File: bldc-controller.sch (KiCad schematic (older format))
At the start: 14 parts, among them U1 STM32F401CBUx

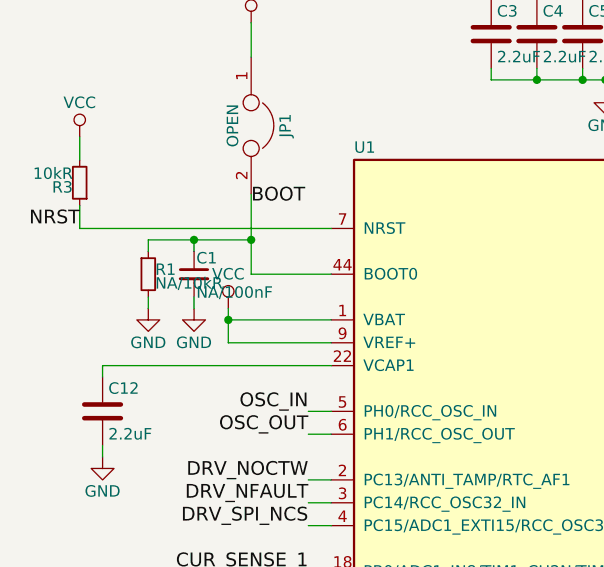
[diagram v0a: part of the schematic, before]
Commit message: even though Im pretty sure that resistor is actually not needed Id like to play safe and have it anyway
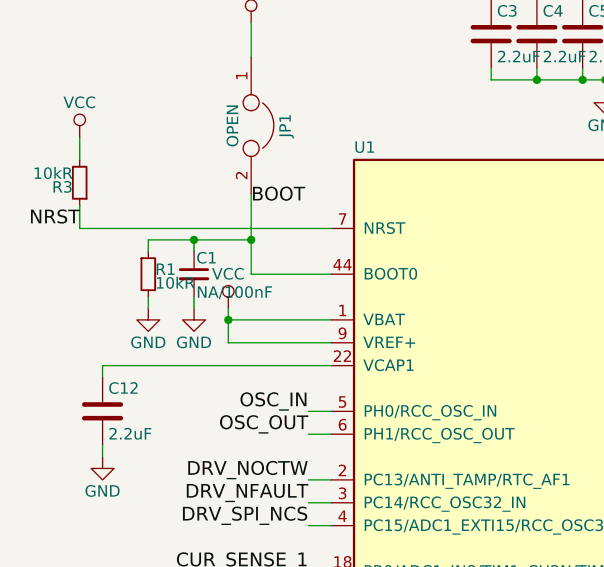
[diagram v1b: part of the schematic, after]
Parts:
- R1: value NA/10kR -> 10kR
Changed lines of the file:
@@
 P 1000 2050
 F 0 "R1" H 1030 2070 50  0000 L CNN
-F 1 "NA/10kR" H 1030 2010 50  0000 L CNN
+F 1 "10kR" H 1030 2010 50  0000 L CNN
 F 2 "Resistors_SMD:R_0603" H 1000 2050 50  0001 C CNN
 F 3 "" H 1000 2050 50  0000 C CNN

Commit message: long forgotten commit of something I did half a year ago -.-
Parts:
- removed JP1: OPEN, Resistors_SMD:R_0402, symbol JUMPER
- added R15: 10kR, Resistor_SMD:R_0603_1608Metric, symbol bldc-controller-rescue:R_Small
- C1: footprint Capacitors_SMD:C_0603 -> Capacitor_SMD:C_0603_1608Metric; symbol C_Small -> bldc-controller-rescue:C_Small
- C10, C12, C3, C4, C5, C6, C7: footprint Capacitors_SMD:C_0603 -> Capacitor_SMD:C_0603_1608Metric; symbol C -> bldc-controller-rescue:C
- D3: footprint LEDs:LED_0805 -> LED_SMD:LED_0805_2012Metric; symbol Led_Small -> bldc-controller-rescue:Led_Small
- R1, R3, R5: footprint Resistors_SMD:R_0603 -> Resistor_SMD:R_0603_1608Metric; symbol R_Small -> bldc-controller-rescue:R_Small
- U1: footprint Housings_DFN_QFN:QFN-48-1EP_7x7mm_Pitch0.5mm -> Package_DFN_QFN:QFN-48-1EP_7x7mm_P0.5mm_EP5.3x5.3mm; symbol STM32F401CBUx -> bldc-controller-rescue:STM32F401CBUx
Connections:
- net BOOT: now also R15.1
- net DRV_L_C: now also U1.28 (PB15/ADC1_EXTI15/I2S2_SD/RTC_REFIN/SPI2_MOSI/TIM1_CH3N); no longer U1.19 (PB1/ADC1_IN9/TIM1_CH3N/TIM3_CH4)
- net LED_MOSI: no longer U1.28 (PB15/ADC1_EXTI15/I2S2_SD/RTC_REFIN/SPI2_MOSI/TIM1_CH3N)
- net VCC: now also R15.2
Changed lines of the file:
@@
-EESchema Schematic File Version 2
-LIBS:bldc-controller-rescue
-LIBS:power
-LIBS:device
-LIBS:transistors
-LIBS:conn
-LIBS:linear
-LIBS:regul
-LIBS:74xx
-LIBS:cmos4000
-LIBS:adc-dac
-LIBS:memory
-LIBS:xilinx
-LIBS:microcontrollers
-LIBS:dsp
-LIBS:microchip
-LIBS:analog_switches
-LIBS:motorola
-LIBS:texas
-LIBS:intel
-LIBS:audio
-LIBS:interface
-LIBS:digital-audio
-LIBS:philips
-LIBS:display
-LIBS:cypress
-LIBS:siliconi
-LIBS:opto
-LIBS:atmel
-LIBS:contrib
-LIBS:valves
-LIBS:Power_Management
-LIBS:st-microelectronics
-LIBS:stm32
-LIBS:w_analog
-LIBS:mpu6000
+EESchema Schematic File Version 4
 LIBS:bldc-controller-cache
-EELAYER 25 0
+EELAYER 29 0
 EELAYER END
 $Descr A4 11693 8268
@@
 $EndDescr
 $Comp
-L VCC #PWR01
+L bldc-controller-rescue:VCC #PWR01
 U 1 1 578D5F23
 P 4900 1350
@@
 $EndComp
 $Comp
-L C C4
+L bldc-controller-rescue:C C4
 U 1 1 578E348A
 P 2700 1000
 F 0 "C4" H 2725 1100 50  0000 L CNN
 F 1 "2.2uF" H 2725 900 50  0000 L CNN
-F 2 "Capacitors_SMD:C_0603" H 2738 850 50  0001 C CNN
+F 2 "Capacitor_SMD:C_0603_1608Metric" H 2738 850 50  0001 C CNN
 F 3 "" H 2700 1000 50  0000 C CNN
 	1    2700 1000
@@
 $EndComp
 $Comp
-L C C5
+L bldc-controller-rescue:C C5
 U 1 1 578E3698
 P 2900 1000
 F 0 "C5" H 2925 1100 50  0000 L CNN
 F 1 "2.2uF" H 2925 900 50  0000 L CNN
-F 2 "Capacitors_SMD:C_0603" H 2938 850 50  0001 C CNN
+F 2 "Capacitor_SMD:C_0603_1608Metric" H 2938 850 50  0001 C CNN
 F 3 "" H 2900 1000 50  0000 C CNN
 	1    2900 1000
@@
 $EndComp
 $Comp
-L C C6
+L bldc-controller-rescue:C C6
 U 1 1 578E36C2
 P 3100 1000
 F 0 "C6" H 3125 1100 50  0000 L CNN
 F 1 "2.2uF" H 3125 900 50  0000 L CNN
-F 2 "Capacitors_SMD:C_0603" H 3138 850 50  0001 C CNN
+F 2 "Capacitor_SMD:C_0603_1608Metric" H 3138 850 50  0001 C CNN
 F 3 "" H 3100 1000 50  0000 C CNN
 	1    3100 1000
@@
 $EndComp
 $Comp
-L C C7
+L bldc-controller-rescue:C C7
 U 1 1 578E36EB
 P 3300 1000
 F 0 "C7" H 3325 1100 50  0000 L CNN
 F 1 "2.2uF" H 3325 900 50  0000 L CNN
-F 2 "Capacitors_SMD:C_0603" H 3338 850 50  0001 C CNN
+F 2 "Capacitor_SMD:C_0603_1608Metric" H 3338 850 50  0001 C CNN
 F 3 "" H 3300 1000 50  0000 C CNN
 	1    3300 1000
@@
 $EndComp
 $Comp
-L C C10
+L bldc-controller-rescue:C C10
 U 1 1 578E3717
 P 3500 1000
 F 0 "C10" H 3525 1100 50  0000 L CNN
 F 1 "2.2uF" H 3525 900 50  0000 L CNN
-F 2 "Capacitors_SMD:C_0603" H 3538 850 50  0001 C CNN
+F 2 "Capacitor_SMD:C_0603_1608Metric" H 3538 850 50  0001 C CNN
 F 3 "" H 3500 1000 50  0000 C CNN
 	1    3500 1000
@@
 $EndComp
 $Comp
-L C C3
+L bldc-controller-rescue:C C3
 U 1 1 578E3746
 P 2500 1000
 F 0 "C3" H 2525 1100 50  0000 L CNN
 F 1 "2.2uF" H 2525 900 50  0000 L CNN
-F 2 "Capacitors_SMD:C_0603" H 2538 850 50  0001 C CNN
+F 2 "Capacitor_SMD:C_0603_1608Metric" H 2538 850 50  0001 C CNN
 F 3 "" H 2500 1000 50  0000 C CNN
 	1    2500 1000
@@
 $EndComp
 $Comp
-L GND #PWR02
+L bldc-controller-rescue:GND #PWR02
 U 1 1 578E393F
 P 3000 1250
@@
 $EndComp
 $Comp
-L VCC #PWR03
+L bldc-controller-rescue:VCC #PWR03
 U 1 1 578E39A1
 P 3000 750
@@
 $EndComp
 $Comp
-L VCC #PWR04
+L bldc-controller-rescue:VCC #PWR04
 U 1 1 578E3BA4
 P 1450 950
@@
 $EndSheet
 $Comp
-L GND #PWR05
+L bldc-controller-rescue:GND #PWR05
 U 1 1 578E83F1
 P 4900 5350
@@
 $EndComp
 $Comp
-L C C12
+L bldc-controller-rescue:C C12
 U 1 1 578E86F2
 P 800 2650
 F 0 "C12" H 825 2750 50  0000 L CNN
 F 1 "2.2uF" H 825 2550 50  0000 L CNN
-F 2 "Capacitors_SMD:C_0603" H 838 2500 50  0001 C CNN
+F 2 "Capacitor_SMD:C_0603_1608Metric" H 838 2500 50  0001 C CNN
 F 3 "" H 800 2650 50  0000 C CNN
 	1    800  2650
@@
 NRST
 $Comp
-L R_Small R5
+L bldc-controller-rescue:R_Small R5
 U 1 1 578F416D
 P 8500 4750
 F 0 "R5" H 8530 4770 50  0000 L CNN
 F 1 "330" H 8530 4710 50  0000 L CNN
-F 2 "Resistors_SMD:R_0603" H 8500 4750 50  0001 C CNN
+F 2 "Resistor_SMD:R_0603_1608Metric" H 8500 4750 50  0001 C CNN
 F 3 "" H 8500 4750 50  0000 C CNN
 	1    8500 4750
@@
 $EndComp
 $Comp
-L Led_Small D3
+L bldc-controller-rescue:Led_Small D3
 U 1 1 578F4224
 P 8850 4750
 F 0 "D3" H 8800 4875 50  0000 L CNN
 F 1 "status" V 8675 4650 50  0000 L CNN
-F 2 "LEDs:LED_0805" V 8850 4750 50  0001 C CNN
+F 2 "LED_SMD:LED_0805_2012Metric" V 8850 4750 50  0001 C CNN
 F 3 "" V 8850 4750 50  0000 C CNN
 	1    8850 4750
@@
 $EndComp
 $Comp
-L VCC #PWR06
+L bldc-controller-rescue:VCC #PWR06
 U 1 1 578F4438
 P 9000 4700
@@
 PWM_2
 $Comp
-L STM32F401CBUx U1
+L bldc-controller-rescue:STM32F401CBUx U1
 U 1 1 5807ABBD
 P 4900 3350
 F 0 "U1" H 1900 5175 50  0000 L BNN
 F 1 "STM32F401CBUx" H 7900 5175 50  0000 R BNN
-F 2 "Housings_DFN_QFN:QFN-48-1EP_7x7mm_Pitch0.5mm" H 7900 5125 50  0000 R TNN
+F 2 "Package_DFN_QFN:QFN-48-1EP_7x7mm_P0.5mm_EP5.3x5.3mm" H 7900 5125 50  0000 R TNN
 F 3 "" H 4900 3350 50  0000 C CNN
 	1    4900 3350
@@
 Text Label 1700 4650 2    60   ~ 0
 DRV_L_B
-Text Label 1700 3450 2    60   ~ 0
-DRV_L_C
 Text Label 8100 4550 0    60   ~ 0
 SWDIO
@@
 SWDCLK
 $Comp
-L GND #PWR07
+L bldc-controller-rescue:GND #PWR07
 U 1 1 580BEB44
 P 800 2850
@@
 $EndComp
 $Comp
-L VCC #PWR08
+L bldc-controller-rescue:VCC #PWR08
 U 1 1 580C0FAE
 P 6500 6900
@@
 Text Label 8100 3650 0    60   ~ 0
 V_PP_SENSE
-$Comp
-L JUMPER JP1
-U 1 1 580CCA9A
-P 1450 1400
-F 0 "JP1" H 1450 1550 50  0000 C CNN
-F 1 "OPEN" H 1450 1320 50  0000 C CNN
-F 2 "Resistors_SMD:R_0402" H 1450 1400 50  0001 C CNN
-F 3 "" H 1450 1400 50  0000 C CNN
-	1    1450 1400
-	0    1    1    0
-$EndComp
 Text Label 8100 3950 0    60   ~ 0
 SENSE_V_1
@@
 SENSE_V_3
 $Comp
-L VCC #PWR09
+L bldc-controller-rescue:VCC #PWR09
 U 1 1 580D5C32
 P 1350 2200
@@
 	4800 1400 4800 1450
 Wire Wire Line
-	4800 1400 5000 1400
-Wire Wire Line
-	4900 1350 4900 1450
+	4800 1400 4900 1400
+Wire Wire Line
+	4900 1350 4900 1400
 Wire Wire Line
 	2200 6200 2300 6200
@@
 	4700 5150 4700 5300
 Wire Wire Line
-	4700 5300 5100 5300
-Wire Wire Line
-	4900 5150 4900 5350
+	4700 5300 4800 5300
+Wire Wire Line
+	4900 5150 4900 5300
 Wire Wire Line
 	1700 2750 1800 2750
@@
 	3500 1200 3500 1150
 Wire Wire Line
-	2500 1200 3500 1200
+	2500 1200 2700 1200
 Connection ~ 2700 800
 Wire Wire Line
@@
 	3500 800  3500 850
 Wire Wire Line
-	2500 800  3500 800
-Wire Wire Line
-	1450 1700 1450 2050
-Wire Wire Line
-	1450 950  1450 1100
+	2500 800  2700 800
 Wire Wire Line
 	700  1850 1800 1850
@@
 	1800 3750 1700 3750
 Wire Wire Line
-	8100 3950 8000 3950
-Wire Wire Line
 	8100 3850 8000 3850
 Wire Wire Line
@@
 	1700 3150 1800 3150
 Wire Wire Line
-	1350 2200 1350 2350
+	1350 2200 1350 2250
 Wire Wire Line
 	1350 2250 1800 2250
@@
 Text Label 1700 2750 2    60   ~ 0
 OSC_OUT
-Text Label 1700 4750 2    60   ~ 0
-LED_MOSI
 Wire Wire Line
 	1700 4750 1800 4750
 $Comp
-L R_Small R3
+L bldc-controller-rescue:R_Small R3
 U 1 1 578E3167
 P 700 1650
 F 0 "R3" H 730 1670 50  0000 L CNN
 F 1 "10kR" H 730 1610 50  0000 L CNN
-F 2 "Resistors_SMD:R_0603" H 700 1650 50  0001 C CNN
+F 2 "Resistor_SMD:R_0603_1608Metric" H 700 1650 50  0001 C CNN
 F 3 "" H 700 1650 50  0000 C CNN
 	1    700  1650
@@
 	1000 2200 1000 2150
 $Comp
-L R_Small R1
+L bldc-controller-rescue:R_Small R1
 U 1 1 580F426E
 P 1000 2050
 F 0 "R1" H 1030 2070 50  0000 L CNN
 F 1 "10kR" H 1030 2010 50  0000 L CNN
-F 2 "Resistors_SMD:R_0603" H 1000 2050 50  0001 C CNN
+F 2 "Resistor_SMD:R_0603_1608Metric" H 1000 2050 50  0001 C CNN
 F 3 "" H 1000 2050 50  0000 C CNN
 	1    1000 2050
@@
 $EndComp
 $Comp
-L GND #PWR010
+L bldc-controller-rescue:GND #PWR010
 U 1 1 580F4274
 P 1000 2200
@@
 	1000 1950 1000 1900
 Wire Wire Line
-	1000 1900 1450 1900
+	1000 1900 1200 1900
 Connection ~ 1450 1900
 $Comp
-L C_Small C1
+L bldc-controller-rescue:C_Small C1
 U 1 1 58126738
 P 1200 2050
 F 0 "C1" H 1210 2120 50  0000 L CNN
 F 1 "NA/100nF" H 1210 1970 50  0000 L CNN
-F 2 "Capacitors_SMD:C_0603" H 1200 2050 50  0001 C CNN
+F 2 "Capacitor_SMD:C_0603_1608Metric" H 1200 2050 50  0001 C CNN
 F 3 "" H 1200 2050 50  0000 C CNN
 	1    1200 2050
@@
 $EndComp
 $Comp
-L GND #PWR011
+L bldc-controller-rescue:GND #PWR011
 U 1 1 58126AD7
 P 1200 2200
@@
 	1700 4350 1800 4350
 $Comp
-L VCC #PWR012
+L bldc-controller-rescue:VCC #PWR012
 U 1 1 58138DD1
 P 700 1450
@@
 	10600 1000 10550 1000
 $Comp
-L VPP #PWR013
+L bldc-controller-rescue:VPP #PWR013
 U 1 1 5817D479
 P 8900 900
@@
 Wire Wire Line
 	8900 1000 9550 1000
+Wire Wire Line
+	4800 5300 4900 5300
+Wire Wire Line
+	5000 5300 5100 5300
+Wire Wire Line
+	4900 1400 5000 1400
+Wire Wire Line
+	4900 1400 4900 1450
+Wire Wire Line
+	4900 5300 4900 5350
+Wire Wire Line
+	4900 5300 5000 5300
+Wire Wire Line
+	3000 800  3100 800
+Wire Wire Line
+	3000 1200 3100 1200
+Wire Wire Line
+	2700 1200 2900 1200
+Wire Wire Line
+	2900 1200 3000 1200
+Wire Wire Line
+	3100 1200 3300 1200
+Wire Wire Line
+	3300 1200 3500 1200
+Wire Wire Line
+	2700 800  2900 800
+Wire Wire Line
+	2900 800  3000 800
+Wire Wire Line
+	3100 800  3300 800
+Wire Wire Line
+	3300 800  3500 800
+Wire Wire Line
+	1350 2250 1350 2350
+Wire Wire Line
+	1450 1900 1450 2050
+Wire Wire Line
+	1200 1900 1450 1900
+$Comp
+L bldc-controller-rescue:R_Small R15
+U 1 1 5D33DD65
+P 1450 1400
+F 0 "R15" H 1480 1420 50  0000 L CNN
+F 1 "10kR" H 1480 1360 50  0000 L CNN
+F 2 "Resistor_SMD:R_0603_1608Metric" H 1450 1400 50  0001 C CNN
+F 3 "" H 1450 1400 50  0000 C CNN
+	1    1450 1400
+	-1   0    0    1
+$EndComp
+Wire Wire Line
+	1450 950  1450 1300
+Wire Wire Line
+	1450 1500 1450 1900
+Wire Wire Line
+	8000 3950 8100 3950
+Text Label 1700 4750 2    60   ~ 0
+DRV_L_C
 $EndSCHEMATC
